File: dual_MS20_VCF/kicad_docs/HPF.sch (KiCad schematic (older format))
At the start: 29 parts, among them Q1 BC558, Q2 BC558, U1 LM13700, U2 MC1458, U3 MC1458

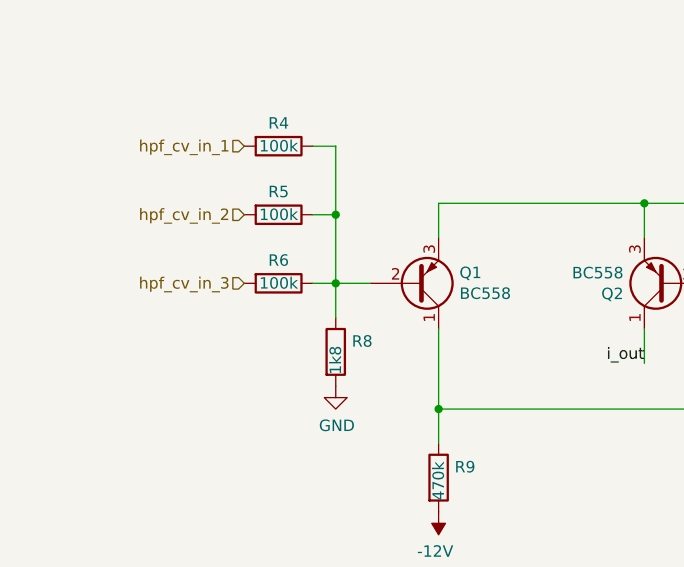
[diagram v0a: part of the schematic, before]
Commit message: change scaling resistors for manual cutoff controls
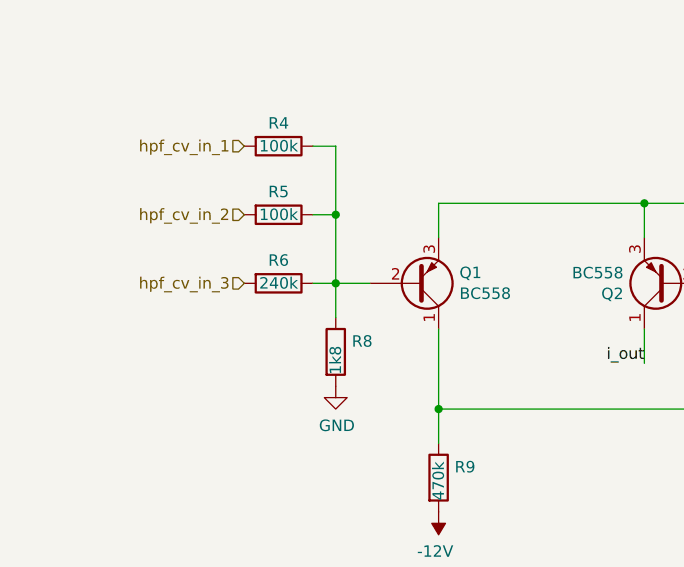
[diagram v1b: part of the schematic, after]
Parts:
- R6: value 100k -> 240k
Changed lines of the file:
@@
 P 2150 6300
 F 0 "R6" V 2050 6300 50  0000 C CNN
-F 1 "100k" V 2150 6300 50  0000 C CNN
+F 1 "240k" V 2150 6300 50  0000 C CNN
 F 2 "Resistor_THT:R_Axial_DIN0207_L6.3mm_D2.5mm_P10.16mm_Horizontal" V 2080 6300 50  0001 C CNN
 F 3 "~" H 2150 6300 50  0001 C CNN
